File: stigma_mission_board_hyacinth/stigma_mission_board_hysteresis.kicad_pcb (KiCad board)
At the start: 2 copper layers, 70 x 110 mm, 51 parts, among them U10 Ai-Thinker-Ra-01, U3 L7805

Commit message: uploaded files to share current not working parts
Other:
- copper layers 2 -> 4
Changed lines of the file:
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@@
 	(generator_version "8.0")
 	(general
-		(thickness 1.6)
+		(thickness 1.6062)
 		(legacy_teardrops no)
 	)
@@
 	(layers
 		(0 "F.Cu" signal)
+		(1 "In1.Cu" signal)
+		(2 "In2.Cu" signal)
 		(31 "B.Cu" signal)
 		(32 "B.Adhes" user "B.Adhesive")
@@
 			)
 			(layer "dielectric 1"
+				(type "prepreg")
+				(thickness 0.2104)
+				(material "FR4")
+				(epsilon_r 4.4)
+				(loss_tangent 0.02)
+			)
+			(layer "In1.Cu"
+				(type "copper")
+				(thickness 0.0152)
+			)
+			(layer "dielectric 2"
 				(type "core")
-				(thickness 1.51)
+				(thickness 1.065)
+				(material "FR4")
+				(epsilon_r 4.6)
+				(loss_tangent 0.02)
+			)
+			(layer "In2.Cu"
+				(type "copper")
+				(thickness 0.0152)
+			)
+			(layer "dielectric 3"
+				(type "prepreg")
+				(thickness 0.2104)
 				(material "FR4")
-				(epsilon_r 4.5)
+				(epsilon_r 4.4)
 				(loss_tangent 0.02)
 			)
@@
 				(color "White")
 			)
-			(copper_finish "Immersion gold")
-			(dielectric_constraints no)
+			(copper_finish "None")
+			(dielectric_constraints yes)
 		)
 		(pad_to_mask_clearance 0)
@@
 		)
 		(property "LCSC#" "C2830749"
-			(at 9.4 158.8 360)
+			(at 9.4 158.8 0)
 			(layer "F.Fab")
 			(hide yes)
@@
 		)
 		(property "Manufacturer" "Ai-Thinker"
-			(at 9.4 158.8 360)
+			(at 9.4 158.8 0)
 			(layer "F.Fab")
 			(hide yes)
@@
 		)
 		(property "Part#" "Ra-01SC"
-			(at 9.4 158.8 360)
+			(at 9.4 158.8 0)
 			(layer "F.Fab")
 			(hide yes)
@@
 		(tags "connector Molex Micro-Fit_3.0 horizontal")
 		(property "Reference" "REF**"
-			(at 1.5 -10.12 360)
+			(at 1.5 -10.12 0)
 			(layer "F.SilkS")
 			(hide yes)
@@
 		)
 		(property "Value" "Molex_Micro-Fit_3.0_43045-0400_2x02_P3.00mm_Horizontal"
-			(at 1.5 5.7 360)
+			(at 1.5 5.7 0)
 			(layer "F.Fab")
 			(hide yes)
@@
 		)
 		(fp_text user "${REFERENCE}"
-			(at 1.5 -8.22 360)
+			(at 1.5 -8.22 0)
 			(layer "F.Fab")
 			(effects
@@
 		(tags "CMT 8504")
 		(property "Reference" "BZ1"
-			(at 0 -2.8 360)
+			(at 0 -2.8 0)
 			(layer "F.SilkS")
 			(effects
@@
 		)
 		(property "Value" "Buzzer"
-			(at 0.1 6 360)
+			(at 0.1 6 0)
 			(layer "F.Fab")
 			(hide yes)
@@
 		)
 		(property "Footprint" ""
-			(at 0 0 360)
+			(at 0 0 0)
 			(layer "F.Fab")
 			(hide yes)
@@
 		)
 		(property "Datasheet" ""
-			(at 0 0 360)
+			(at 0 0 0)
 			(layer "F.Fab")
 			(hide yes)
@@
 		)
 		(property "Description" "Buzzer, polarized"
-			(at 0 0 360)
+			(at 0 0 0)
 			(layer "F.Fab")
 			(hide yes)
@@
 		)
 		(property "DigiKey#" "102-CMT-8504-100-SMT-CT-ND"
-			(at 0 0 360)
+			(at 0 0 0)
 			(layer "F.Fab")
 			(hide yes)
@@
 		)
 		(property "LCSC#" "C781886"
-			(at 0 0 360)
+			(at 0 0 0)
 			(layer "F.Fab")
 			(hide yes)
@@
 		)
 		(property "Manufacturer" "CUI Devices"
-			(at 0 0 360)
+			(at 0 0 0)
 			(layer "F.Fab")
 			(hide yes)
@@
 		)
 		(property "Notes" "(or YUEXIN YX-SMD8530P from LCSC)"
-			(at 0 0 360)
+			(at 0 0 0)
 			(layer "F.Fab")
 			(hide yes)
@@
 		)
 		(property "Part#" "CMT-8504-100-SMT-TR"
-			(at 0 0 360)
+			(at 0 0 0)
 			(layer "F.Fab")
 			(hide yes)
@@
 		)
 		(fp_text user "${REFERENCE}"
-			(at 0.1 1.7 360)
+			(at 0.1 1.7 0)
 			(layer "F.Fab")
 			(hide yes)
@@
 		(tags "resistor")
 		(property "Reference" "R1"
-			(at 4.55 0 360)
+			(at 4.55 0 0)
 			(layer "F.SilkS")
 			(effects
@@
 		(tags "DPAK TO-252 DPAK-3 TO-252-3 SOT-428")
 		(property "Reference" "U3"
-			(at -4.349999 0 360)
+			(at -4.349999 0 0)
 			(layer "F.SilkS")
 			(effects
@@
 		(tags "Through hole pin header THT 1x02 2.54mm single row")
 		(property "Reference" "REF**"
-			(at 0 -2.33 360)
+			(at 0 -2.33 0)
 			(layer "F.SilkS")
 			(effects
@@
 		)
 		(property "Value" "PinHeader_1x02_P2.54mm_Vertical"
-			(at 0 4.87 360)
+			(at 0 4.87 0)
 			(layer "F.Fab")
 			(effects

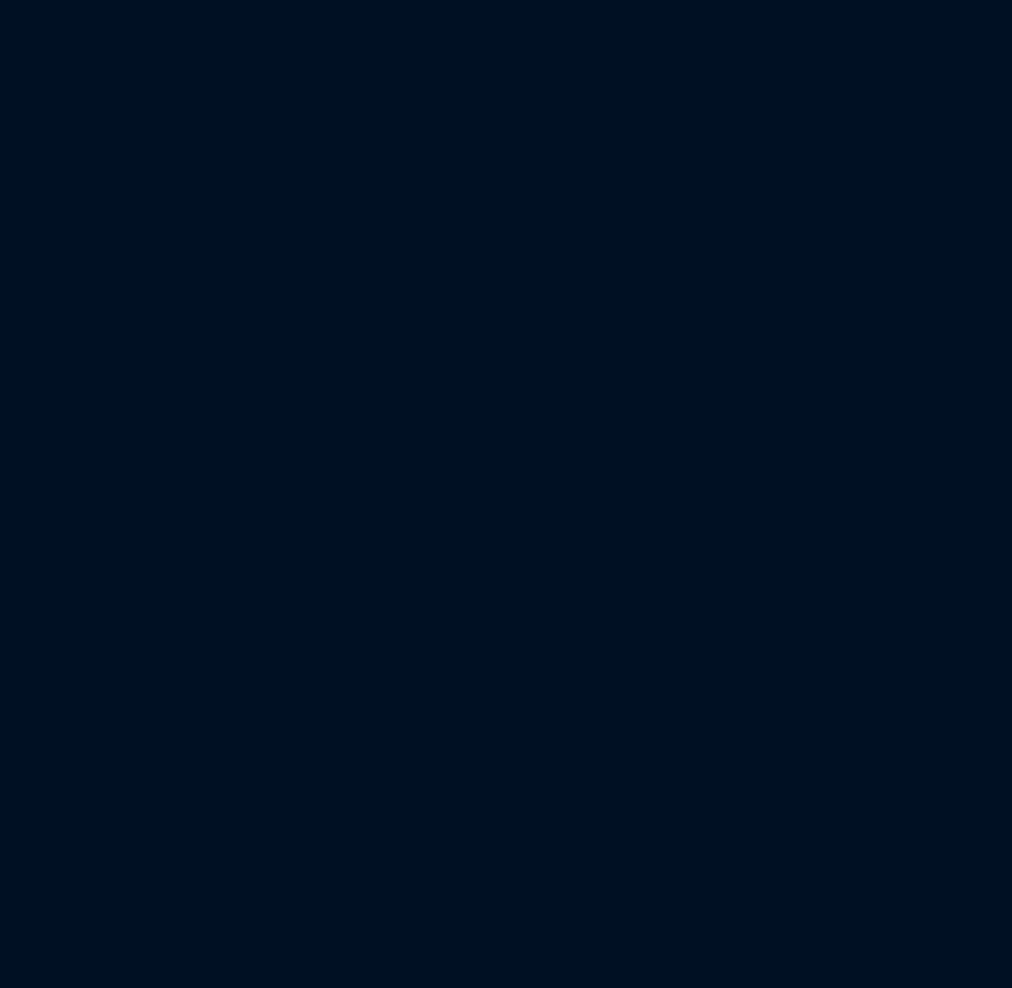
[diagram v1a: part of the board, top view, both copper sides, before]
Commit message: Added missing Footprints and changed GPS Connector
into the right directory this time
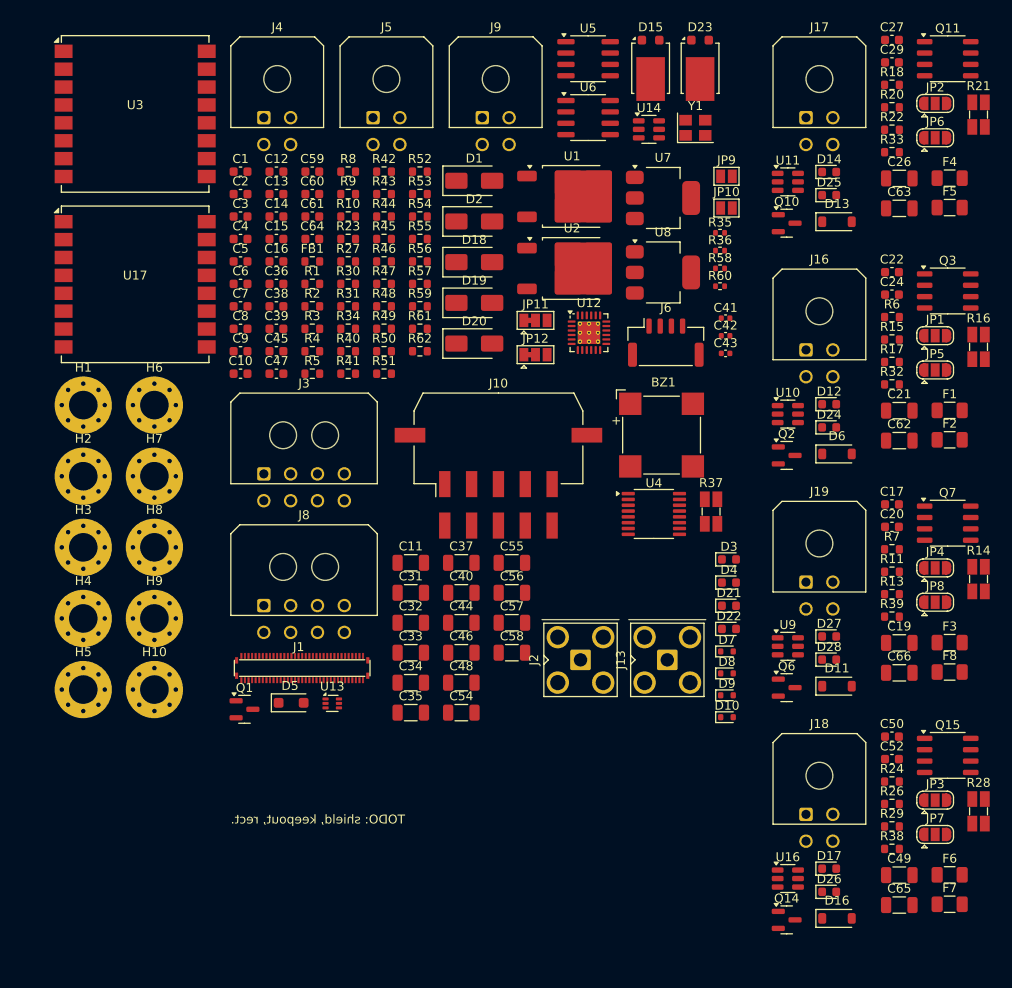
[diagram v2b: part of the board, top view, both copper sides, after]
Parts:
- added BZ1: Buzzer, Buzzer_Beeper:MagneticBuzzer_CUI_CMT-8504-100-SMT, F.Cu at (212.4, 79.3)
- added C1: 330n, Capacitor_SMD:C_0603_1608Metric, F.Cu at (165.3, 49.9)
- added C10: DNP, Capacitor_SMD:C_0603_1608Metric, F.Cu at (165.3, 72.5)
- added C11: 10u, Capacitor_SMD:C_1206_3216Metric, F.Cu at (184.3, 93.6)
- added C12: 10u, Capacitor_SMD:C_0603_1608Metric, F.Cu at (169.3, 49.9)
- added C13: 22u, Capacitor_SMD:C_0603_1608Metric, F.Cu at (169.3, 52.4)
- added C14: 10u, Capacitor_SMD:C_0603_1608Metric, F.Cu at (169.3, 54.9)
- added C15: 22u, Capacitor_SMD:C_0603_1608Metric, F.Cu at (169.3, 57.4)
- added C16: 100n, Capacitor_SMD:C_0603_1608Metric, F.Cu at (169.3, 59.9)
- added C17: 100n, Capacitor_SMD:C_0603_1608Metric, F.Cu at (238.1, 87.1)
- added C19: 10u, Capacitor_SMD:C_1206_3216Metric, F.Cu at (238.9, 102.6)
- added C2: 330n, Capacitor_SMD:C_0603_1608Metric, F.Cu at (165.3, 52.4)
- added C20: 100n, Capacitor_SMD:C_0603_1608Metric, F.Cu at (238.1, 89.6)
- added C21: 10u, Capacitor_SMD:C_1206_3216Metric, F.Cu at (238.9, 76.6)
- added C22: 100n, Capacitor_SMD:C_0603_1608Metric, F.Cu at (238.1, 61.1)
- added C24: 100n, Capacitor_SMD:C_0603_1608Metric, F.Cu at (238.1, 63.6)
- added C26: 10u, Capacitor_SMD:C_1206_3216Metric, F.Cu at (238.9, 50.6)
- added C27: 100n, Capacitor_SMD:C_0603_1608Metric, F.Cu at (238.1, 35.2)
- added C29: 100n, Capacitor_SMD:C_0603_1608Metric, F.Cu at (238.1, 37.7)
- added C3: 100n, Capacitor_SMD:C_0603_1608Metric, F.Cu at (165.3, 54.9)
- added C31: 22u, Capacitor_SMD:C_1206_3216Metric, F.Cu at (184.3, 97.0)
- added C32: 1u, Capacitor_SMD:C_1206_3216Metric, F.Cu at (184.3, 100.3)
- added C33: 10u, Capacitor_SMD:C_1206_3216Metric, F.Cu at (184.3, 103.7)
- added C34: 10u, Capacitor_SMD:C_1206_3216Metric, F.Cu at (184.3, 107.0)
- added C35: 22u, Capacitor_SMD:C_1206_3216Metric, F.Cu at (184.3, 110.4)
- added C36: 100n, Capacitor_SMD:C_0603_1608Metric, F.Cu at (169.3, 62.4)
- added C37: 10u, Capacitor_SMD:C_1206_3216Metric, F.Cu at (190.0, 93.6)
- added C38: 100n, Capacitor_SMD:C_0603_1608Metric, F.Cu at (169.3, 64.9)
- added C39: 100n, Capacitor_SMD:C_0603_1608Metric, F.Cu at (169.3, 67.4)
- added C4: 100n, Capacitor_SMD:C_0603_1608Metric, F.Cu at (165.3, 57.4)
- added C40: 1u, Capacitor_SMD:C_1206_3216Metric, F.Cu at (190.0, 97.0)
- added C41: 470p, Capacitor_SMD:C_0402_1005Metric, F.Cu at (219.5, 66.3)
- added C42: 10p, Capacitor_SMD:C_0402_1005Metric, F.Cu at (219.5, 68.2)
- added C43: 10p, Capacitor_SMD:C_0402_1005Metric, F.Cu at (219.5, 70.2)
- added C44: 10u, Capacitor_SMD:C_1206_3216Metric, F.Cu at (190.0, 100.3)
- added C45: 100n, Capacitor_SMD:C_0603_1608Metric, F.Cu at (169.3, 70.0)
- added C46: 1u, Capacitor_SMD:C_1206_3216Metric, F.Cu at (190.0, 103.7)
- added C47: 100n, Capacitor_SMD:C_0603_1608Metric, F.Cu at (169.3, 72.5)
- added C48: 22u, Capacitor_SMD:C_1206_3216Metric, F.Cu at (190.0, 107.0)
- added C49: 10u, Capacitor_SMD:C_1206_3216Metric, F.Cu at (238.9, 128.5)
- added C5: DNP, Capacitor_SMD:C_0603_1608Metric, F.Cu at (165.3, 59.9)
- added C50: 100n, Capacitor_SMD:C_0603_1608Metric, F.Cu at (238.1, 113.0)
- added C52: 100n, Capacitor_SMD:C_0603_1608Metric, F.Cu at (238.1, 115.5)
- added C54: 22u, Capacitor_SMD:C_1206_3216Metric, F.Cu at (190.0, 110.4)
- added C55: 22u, Capacitor_SMD:C_1206_3216Metric, F.Cu at (195.6, 93.6)
- added C56: 22u, Capacitor_SMD:C_1206_3216Metric, F.Cu at (195.6, 97.0)
- added C57: 4u7, Capacitor_SMD:C_1206_3216Metric, F.Cu at (195.6, 100.3)
- added C58: 4u7, Capacitor_SMD:C_1206_3216Metric, F.Cu at (195.6, 103.7)
- added C59: 100n, Capacitor_SMD:C_0603_1608Metric, F.Cu at (173.3, 49.9)
- added C6: DNP, Capacitor_SMD:C_0603_1608Metric, F.Cu at (165.3, 62.4)
- added C60: 100n, Capacitor_SMD:C_0603_1608Metric, F.Cu at (173.3, 52.4)
- added C61: 100n, Capacitor_SMD:C_0603_1608Metric, F.Cu at (173.3, 54.9)
- added C62: 10u, Capacitor_SMD:C_1206_3216Metric, F.Cu at (238.9, 79.9)
- added C63: 10u, Capacitor_SMD:C_1206_3216Metric, F.Cu at (238.9, 54.0)
- added C64: 100n, Capacitor_SMD:C_0603_1608Metric, F.Cu at (173.3, 57.4)
- added C65: 10u, Capacitor_SMD:C_1206_3216Metric, F.Cu at (238.9, 131.9)
- added C66: 10u, Capacitor_SMD:C_1206_3216Metric, F.Cu at (238.9, 105.9)
- added C7: 100n, Capacitor_SMD:C_0603_1608Metric, F.Cu at (165.3, 64.9)
- added C8: C, Capacitor_SMD:C_0603_1608Metric, F.Cu at (165.3, 67.4)
- added C9: DNP, Capacitor_SMD:C_0603_1608Metric, F.Cu at (165.3, 70.0)
- added D1: SS34, Diode_SMD:D_SMA, F.Cu at (191.4, 50.9)
- added D10: ESD5Zxx, Diode_SMD:D_SOD-523, F.Cu at (219.7, 110.9)
- added D11: NRVB130T1G, Diode_SMD:D_SOD-123, F.Cu at (232.0, 107.4)
- added D12: LED, LED_SMD:LED_0603_1608Metric, F.Cu at (231.1, 75.9)
- added D13: NRVB130T1G, Diode_SMD:D_SOD-123, F.Cu at (232.0, 55.5)
- added D14: LED, LED_SMD:LED_0603_1608Metric, F.Cu at (231.1, 49.9)
- added D15: SVT12100, Package_TO_SOT_SMD:TO-277B, F.Cu at (211.1, 38.3)
- added D16: NRVB130T1G, Diode_SMD:D_SOD-123, F.Cu at (232.0, 133.4)
- added D17: LED, LED_SMD:LED_0603_1608Metric, F.Cu at (231.1, 127.8)
- added D18: SS34, Diode_SMD:D_SMA, F.Cu at (191.4, 60.0)
- added D19: SS34, Diode_SMD:D_SMA, F.Cu at (191.4, 64.5)
- added D2: SS34, Diode_SMD:D_SMA, F.Cu at (191.4, 55.4)
- added D20: SS34, Diode_SMD:D_SMA, F.Cu at (191.4, 69.1)
- added D21: red, LED_SMD:LED_0603_1608Metric, F.Cu at (219.9, 98.4)
- added D22: red, LED_SMD:LED_0603_1608Metric, F.Cu at (219.9, 101.0)
- added D23: SVT12100, Package_TO_SOT_SMD:TO-277B, F.Cu at (216.7, 38.3)
- added D24: D, Diode_SMD:D_0603_1608Metric, F.Cu at (231.1, 78.5)
- added D25: D, Diode_SMD:D_0603_1608Metric, F.Cu at (231.1, 52.5)
- added D26: D, Diode_SMD:D_0603_1608Metric, F.Cu at (231.1, 130.4)
- added D27: D, Diode_SMD:D_0603_1608Metric, F.Cu at (231.1, 101.8)
- added D28: LED, LED_SMD:LED_0603_1608Metric, F.Cu at (231.1, 104.4)
- added D3: red, LED_SMD:LED_0603_1608Metric, F.Cu at (219.9, 93.2)
- added D4: red, LED_SMD:LED_0603_1608Metric, F.Cu at (219.9, 95.8)
- added D5: ~, Diode_SMD:D_SOD-123F, F.Cu at (171.0, 109.3)
- added D6: NRVB130T1G, Diode_SMD:D_SOD-123, F.Cu at (232.0, 81.4)
- added D7: ESD5Zxx, Diode_SMD:D_SOD-523, F.Cu at (219.7, 103.5)
- added D8: ESD5Zxx, Diode_SMD:D_SOD-523, F.Cu at (219.7, 106.0)
- added D9: ESD5Zxx, Diode_SMD:D_SOD-523, F.Cu at (219.7, 108.4)
- added F1: 10A, Fuse:Fuse_1206_3216Metric, F.Cu at (244.6, 76.6)
- added F2: 100mA, Fuse:Fuse_1206_3216Metric, F.Cu at (244.6, 79.9)
- added F3: 10A, Fuse:Fuse_1206_3216Metric, F.Cu at (244.6, 102.5)
- added F4: 100mA, Fuse:Fuse_1206_3216Metric, F.Cu at (244.6, 50.6)
- added F5: 10A, Fuse:Fuse_1206_3216Metric, F.Cu at (244.6, 53.9)
- added F6: 100mA, Fuse:Fuse_1206_3216Metric, F.Cu at (244.6, 128.5)
- added F7: 10A, Fuse:Fuse_1206_3216Metric, F.Cu at (244.6, 131.8)
- added F8: 100mA, Fuse:Fuse_1206_3216Metric, F.Cu at (244.6, 105.8)
- added FB1: FerriteBead, Resistor_SMD:R_0603_1608Metric, F.Cu at (173.3, 59.9)
- added H1: MountingHole_Pad, MountingHole:MountingHole_3.2mm_M3_Pad_Via, F.Cu at (147.7, 76.0)
- added H10: MountingHole_Pad, MountingHole:MountingHole_3.2mm_M3_Pad_Via, F.Cu at (155.7, 107.8)
- added H2: MountingHole_Pad, MountingHole:MountingHole_3.2mm_M3_Pad_Via, F.Cu at (147.7, 83.9)
- added H3: MountingHole_Pad, MountingHole:MountingHole_3.2mm_M3_Pad_Via, F.Cu at (147.7, 91.9)
- added H4: MountingHole_Pad, MountingHole:MountingHole_3.2mm_M3_Pad_Via, F.Cu at (147.7, 99.8)
- added H5: MountingHole_Pad, MountingHole:MountingHole_3.2mm_M3_Pad_Via, F.Cu at (147.7, 107.8)
- added H6: MountingHole_Pad, MountingHole:MountingHole_3.2mm_M3_Pad_Via, F.Cu at (155.7, 76.0)
- added H7: MountingHole_Pad, MountingHole:MountingHole_3.2mm_M3_Pad_Via, F.Cu at (155.7, 83.9)
- added H8: MountingHole_Pad, MountingHole:MountingHole_3.2mm_M3_Pad_Via, F.Cu at (155.7, 91.9)
- added H9: MountingHole_Pad, MountingHole:MountingHole_3.2mm_M3_Pad_Via, F.Cu at (155.7, 99.8)
- added J1: ~, Stigma:DF40GB-70DP-0.4V-plug, F.Cu at (172.2, 105.4)
- added J10: Conn_02x05_Top_Bottom_MountingPin, Connector_Molex:Molex_Micro-Fit_3.0_43045-1010_2x05-1MP_P3.00mm_Horizontal, F.Cu at (194.1, 87.1)
- added J13: SMA, Connector_Coaxial:SMA_Amphenol_901-143_Horizontal, F.Cu at (213.0, 104.5)
- added J16: Conn_02x02_Top_Bottom, Connector_Molex:Molex_Micro-Fit_3.0_43045-0400_2x02_P3.00mm_Horizontal, F.Cu at (228.5, 69.8)
- added J17: Conn_02x02_Top_Bottom, Connector_Molex:Molex_Micro-Fit_3.0_43045-0400_2x02_P3.00mm_Horizontal, F.Cu at (228.5, 43.8)
- added J18: Conn_02x02_Top_Bottom, Connector_Molex:Molex_Micro-Fit_3.0_43045-0400_2x02_P3.00mm_Horizontal, F.Cu at (228.5, 121.7)
- added J19: Conn_02x02_Top_Bottom, Connector_Molex:Molex_Micro-Fit_3.0_43045-0400_2x02_P3.00mm_Horizontal, F.Cu at (228.5, 95.8)
- added J2: SMA, Connector_Coaxial:SMA_Amphenol_901-143_Horizontal, F.Cu at (203.3, 104.5)
- added J3: Conn_02x04_Top_Bottom, Connector_Molex:Molex_Micro-Fit_3.0_43045-0800_2x04_P3.00mm_Horizontal, F.Cu at (167.9, 83.7)
- added J4: ~, Connector_Molex:Molex_Micro-Fit_3.0_43045-0400_2x02_P3.00mm_Horizontal, F.Cu at (167.9, 43.8)
- added J5: Conn_02x02_Top_Bottom, Connector_Molex:Molex_Micro-Fit_3.0_43045-0400_2x02_P3.00mm_Horizontal, F.Cu at (180.1, 43.8)
- added J6: JST-GH, Connector_JST:JST_GH_SM04B-GHS-TB_1x04-1MP_P1.25mm_Horizontal, F.Cu at (212.8, 69.0)
- added J8: Conn_02x04_Top_Bottom, Connector_Molex:Molex_Micro-Fit_3.0_43045-0800_2x04_P3.00mm_Horizontal, F.Cu at (167.9, 98.4)
- added J9: ~, Connector_Molex:Molex_Micro-Fit_3.0_43045-0400_2x02_P3.00mm_Horizontal, F.Cu at (192.3, 43.8)
- added JP1: servo_switch, Jumper:SolderJumper-3_P1.3mm_Open_RoundedPad1.0x1.5mm, F.Cu at (242.9, 68.2)
- added JP10: SolderJumper_2_Open, Jumper:SolderJumper-2_P1.3mm_Open_Pad1.0x1.5mm, F.Cu at (219.6, 53.9)
- added JP11: SolderJumper_3_Bridged12, Jumper:SolderJumper-3_P1.3mm_Bridged12_Pad1.0x1.5mm, F.Cu at (198.3, 66.5)
- added JP12: SolderJumper_3_Bridged12, Jumper:SolderJumper-3_P1.3mm_Bridged12_Pad1.0x1.5mm, F.Cu at (198.3, 70.3)
- added JP2: servo_switch, Jumper:SolderJumper-3_P1.3mm_Open_RoundedPad1.0x1.5mm, F.Cu at (242.9, 42.3)
- added JP3: servo_switch, Jumper:SolderJumper-3_P1.3mm_Open_RoundedPad1.0x1.5mm, F.Cu at (242.9, 120.1)
- added JP4: servo_switch, Jumper:SolderJumper-3_P1.3mm_Open_RoundedPad1.0x1.5mm, F.Cu at (242.9, 94.2)
- added JP5: servo_switch, Jumper:SolderJumper-3_P1.3mm_Open_RoundedPad1.0x1.5mm, F.Cu at (242.9, 72.0)
- added JP6: servo_switch, Jumper:SolderJumper-3_P1.3mm_Open_RoundedPad1.0x1.5mm, F.Cu at (242.9, 46.1)
- added JP7: servo_switch, Jumper:SolderJumper-3_P1.3mm_Open_RoundedPad1.0x1.5mm, F.Cu at (242.9, 124.0)
- added JP8: servo_switch, Jumper:SolderJumper-3_P1.3mm_Open_RoundedPad1.0x1.5mm, F.Cu at (242.9, 98.0)
- added JP9: SolderJumper_2_Open, Jumper:SolderJumper-2_P1.3mm_Open_Pad1.0x1.5mm, F.Cu at (219.6, 50.4)
- added Q1: DMN2056U, Package_TO_SOT_SMD:SOT-23, F.Cu at (165.7, 110.0)
- added Q10: DMN2056U, Package_TO_SOT_SMD:SOT-23, F.Cu at (226.3, 55.6)
- added Q11: AOSP21321, Package_SO:SO-8_3.9x4.9mm_P1.27mm, F.Cu at (244.3, 37.3)
- added Q14: DMN2056U, Package_TO_SOT_SMD:SOT-23, F.Cu at (226.3, 133.5)
- added Q15: AOSP21321, Package_SO:SO-8_3.9x4.9mm_P1.27mm, F.Cu at (244.3, 115.1)
- added Q2: DMN2056U, Package_TO_SOT_SMD:SOT-23, F.Cu at (226.3, 81.6)
- added Q3: AOSP21321, Package_SO:SO-8_3.9x4.9mm_P1.27mm, F.Cu at (244.3, 63.2)
- added Q6: DMN2056U, Package_TO_SOT_SMD:SOT-23, F.Cu at (226.3, 107.6)
- added Q7: AOSP21321, Package_SO:SO-8_3.9x4.9mm_P1.27mm, F.Cu at (244.3, 89.2)
- added R1: 220, Resistor_SMD:R_0603_1608Metric, F.Cu at (173.3, 62.4)
- added R10: 120, DNP, Resistor_SMD:R_0603_1608Metric, F.Cu at (177.3, 54.9)
- added R11: 1k, Resistor_SMD:R_0603_1608Metric, F.Cu at (238.1, 94.6)
- added R13: 60R, Resistor_SMD:R_0603_1608Metric, F.Cu at (238.1, 97.1)
- added R14: 100mR 1%, Resistor_SMD:R_Shunt_Ohmite_LVK12, F.Cu at (247.8, 95.4)
- added R15: 60R, Resistor_SMD:R_0603_1608Metric, F.Cu at (238.1, 68.6)
- added R16: 100mR 1%, Resistor_SMD:R_Shunt_Ohmite_LVK12, F.Cu at (247.8, 69.5)
- added R17: 1k, Resistor_SMD:R_0603_1608Metric, F.Cu at (238.1, 71.2)
- added R18: 1k, Resistor_SMD:R_0603_1608Metric, F.Cu at (238.1, 40.2)
- added R2: 220, Resistor_SMD:R_0603_1608Metric, F.Cu at (173.3, 64.9)
- added R20: 60R, Resistor_SMD:R_0603_1608Metric, F.Cu at (238.1, 42.7)
- added R21: 100mR 1%, Resistor_SMD:R_Shunt_Ohmite_LVK12, F.Cu at (247.8, 43.5)
- added R22: 1k, Resistor_SMD:R_0603_1608Metric, F.Cu at (238.1, 45.2)
- added R23: 100k, Resistor_SMD:R_0603_1608Metric, F.Cu at (177.3, 57.4)
- added R24: 1k, Resistor_SMD:R_0603_1608Metric, F.Cu at (238.1, 118.1)
- added R26: 60R, Resistor_SMD:R_0603_1608Metric, F.Cu at (238.1, 120.6)
- added R27: 10k, Resistor_SMD:R_0603_1608Metric, F.Cu at (177.3, 59.9)
- added R28: 100mR 1%, Resistor_SMD:R_Shunt_Ohmite_LVK12, F.Cu at (247.8, 121.4)
- added R29: 1k, Resistor_SMD:R_0603_1608Metric, F.Cu at (238.1, 123.1)
- added R3: 0, Resistor_SMD:R_0603_1608Metric, F.Cu at (173.3, 67.4)
- added R30: 100k, Resistor_SMD:R_0603_1608Metric, F.Cu at (177.3, 62.4)
- added R31: 10k, Resistor_SMD:R_0603_1608Metric, F.Cu at (177.3, 64.9)
- added R32: 10k, Resistor_SMD:R_0603_1608Metric, F.Cu at (238.1, 73.7)
- added R33: 10k, Resistor_SMD:R_0603_1608Metric, F.Cu at (238.1, 47.7)
- added R34: 12.1k, Resistor_SMD:R_0603_1608Metric, F.Cu at (177.3, 67.4)
- added R35: 0, Resistor_SMD:R_0402_1005Metric, F.Cu at (218.9, 56.7)
- added R36: 0, Resistor_SMD:R_0402_1005Metric, F.Cu at (218.9, 58.7)
- added R37: 100mR 1%, Resistor_SMD:R_Shunt_Ohmite_LVK12, F.Cu at (217.9, 87.9)
- added R38: 10k, Resistor_SMD:R_0603_1608Metric, F.Cu at (238.1, 125.6)
- added R39: 10k, Resistor_SMD:R_0603_1608Metric, F.Cu at (238.1, 99.6)
- added R4: R, Resistor_SMD:R_0603_1608Metric, F.Cu at (173.3, 70.0)
- added R40: @todo, Resistor_SMD:R_0603_1608Metric, F.Cu at (177.3, 70.0)
- added R41: 50R, Resistor_SMD:R_0603_1608Metric, F.Cu at (177.3, 72.5)
- added R42: 50R, Resistor_SMD:R_0603_1608Metric, F.Cu at (181.3, 49.9)
- added R43: 50R, Resistor_SMD:R_0603_1608Metric, F.Cu at (181.3, 52.4)
- added R44: 50R, Resistor_SMD:R_0603_1608Metric, F.Cu at (181.3, 54.9)
- added R45: 33R, Resistor_SMD:R_0603_1608Metric, F.Cu at (181.3, 57.4)
- added R46: 10k, Resistor_SMD:R_0603_1608Metric, F.Cu at (181.3, 59.9)
- added R47: 10k, Resistor_SMD:R_0603_1608Metric, F.Cu at (181.3, 62.4)
- added R48: 10k, Resistor_SMD:R_0603_1608Metric, F.Cu at (181.3, 64.9)
- added R49: 33R, Resistor_SMD:R_0603_1608Metric, F.Cu at (181.3, 67.4)
- added R5: 0, Resistor_SMD:R_0603_1608Metric, F.Cu at (173.3, 72.5)
- added R50: 10k, Resistor_SMD:R_0603_1608Metric, F.Cu at (181.3, 70.0)
- added R51: 33R, Resistor_SMD:R_0603_1608Metric, F.Cu at (181.3, 72.5)
- added R52: 0, Resistor_SMD:R_0603_1608Metric, F.Cu at (185.3, 49.9)
- added R53: 1k5, Resistor_SMD:R_0603_1608Metric, F.Cu at (185.3, 52.4)
- added R54: 33R, Resistor_SMD:R_0603_1608Metric, F.Cu at (185.3, 54.9)
- added R55: 10k, Resistor_SMD:R_0603_1608Metric, F.Cu at (185.3, 57.4)
- added R56: 10k, Resistor_SMD:R_0603_1608Metric, F.Cu at (185.3, 59.9)
- added R57: 150R, Resistor_SMD:R_0603_1608Metric, F.Cu at (185.3, 62.4)
- added R58: 310R, Resistor_SMD:R_0402_1005Metric, F.Cu at (218.9, 60.7)
- added R59: 150R, Resistor_SMD:R_0603_1608Metric, F.Cu at (185.3, 64.9)
- added R6: 1k, Resistor_SMD:R_0603_1608Metric, F.Cu at (238.1, 66.1)
- added R60: 310R, Resistor_SMD:R_0402_1005Metric, F.Cu at (218.9, 62.7)
- added R61: 220, Resistor_SMD:R_0603_1608Metric, F.Cu at (185.3, 67.4)
- added R62: 220, Resistor_SMD:R_0603_1608Metric, F.Cu at (185.3, 70.0)
- added R7: 1k, Resistor_SMD:R_0603_1608Metric, F.Cu at (238.1, 92.1)
- added R8: 10k, Resistor_SMD:R_0603_1608Metric, F.Cu at (177.3, 49.9)
- added R9: 120, DNP, Resistor_SMD:R_0603_1608Metric, F.Cu at (177.3, 52.4)
- added U1: L7805, Package_TO_SOT_SMD:TO-252-2, F.Cu at (202.4, 52.6)
- added U10: INA181, Package_TO_SOT_SMD:SOT-23-6, F.Cu at (226.5, 77.0)
- added U11: INA181, Package_TO_SOT_SMD:SOT-23-6, F.Cu at (226.5, 51.0)
- added U12: LAN8742A, Package_DFN_QFN:VQFN-24-1EP_4x4mm_P0.5mm_EP2.5x2.5mm_ThermalVias, F.Cu at (204.2, 67.9)
- added U13: TPD4E1U06, Package_TO_SOT_SMD:SOT-563, F.Cu at (175.6, 109.3)
- added U14: INA181, Package_TO_SOT_SMD:SOT-23-6, F.Cu at (210.9, 45.1)
- added U16: INA181, Package_TO_SOT_SMD:SOT-23-6, F.Cu at (226.5, 128.9)
- added U17: Ai-Thinker-Ra-01, RF_Module:Ai-Thinker-Ra-01-LoRa, F.Cu at (153.5, 62.5)
- added U2: L7805, Package_TO_SOT_SMD:TO-252-2, F.Cu at (202.4, 60.7)
- added U3: Ai-Thinker-Ra-01, RF_Module:Ai-Thinker-Ra-01-LoRa, F.Cu at (153.5, 43.4)
- added U4: SN74HCS594, Package_SO:TSSOP-16_4.4x5mm_P0.65mm, F.Cu at (211.5, 88.1)
- added U5: MCP2562-E-SN, Package_SO:SOIC-8_3.9x4.9mm_P1.27mm, F.Cu at (204.2, 37.3)
- added U6: MCP2562-E-SN, Package_SO:SOIC-8_3.9x4.9mm_P1.27mm, F.Cu at (204.2, 43.8)
- added U7: AZ1117H-ADJ, Package_TO_SOT_SMD:SOT-223-3_TabPin2, F.Cu at (212.5, 52.8)
- added U8: AZ1117H-ADJ, Package_TO_SOT_SMD:SOT-223-3_TabPin2, F.Cu at (212.5, 61.1)
- added U9: INA181, Package_TO_SOT_SMD:SOT-23-6, F.Cu at (226.5, 102.9)
- added Y1: 25MHz, Crystal:Crystal_SMD_3225-4Pin_3.2x2.5mm, F.Cu at (216.2, 45.0)
